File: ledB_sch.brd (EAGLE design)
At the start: 22.9 x 22.9 mm, 7 parts

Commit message: add image and fix schema
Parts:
- removed JP2: S+ S-, microbuilder:1X02_OVAL
- added U1: PIEZO, ledB_sch:1X02_PEIZO
- OPAMP: device linear:DIL08 -> ledB_sch:DIL08
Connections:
- net GND: now also R1.1, U1.1; no longer JP2.2
- net SIG: now also U1.2; no longer JP2.1
- net VCC: no longer R1.1
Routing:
- net SIG: track 25.0 -> 15.1 mm
- net GND: track 29.8 -> 26.2 mm
- net VCC: track 25.4 -> 22.2 mm

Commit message: add image and fix schema 2
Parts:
- moved JP1 16.6 mm to (11.0, 19.7), turned to 0 degrees
- moved LED1 16.4 mm to (11.0, 3.24), turned to 180 degrees
- moved D1 16.1 mm to (17.4, 7.05), turned to 90 degrees
- moved R2 14.8 mm to (18.4, 14.9), turned to 115 degrees
- moved R1 13.1 mm to (4.28, 7.16), turned to 115 degrees
- moved U1 12.1 mm to (3.57, 15.5), turned to 78 degrees
- moved OPAMP 1.47 mm to (11.0, 12.1), turned to 270 degrees
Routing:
- net N$1: track 3.59 -> 26.7 mm
- net VCC: track 22.2 -> 14.9 mm
- net N$5: track 10.1 -> 5.59 mm
- net GND: track 26.2 -> 30.1 mm
- net N$2: track 9.97 -> 6.47 mm
- net SIG: track 15.1 -> 16.9 mm

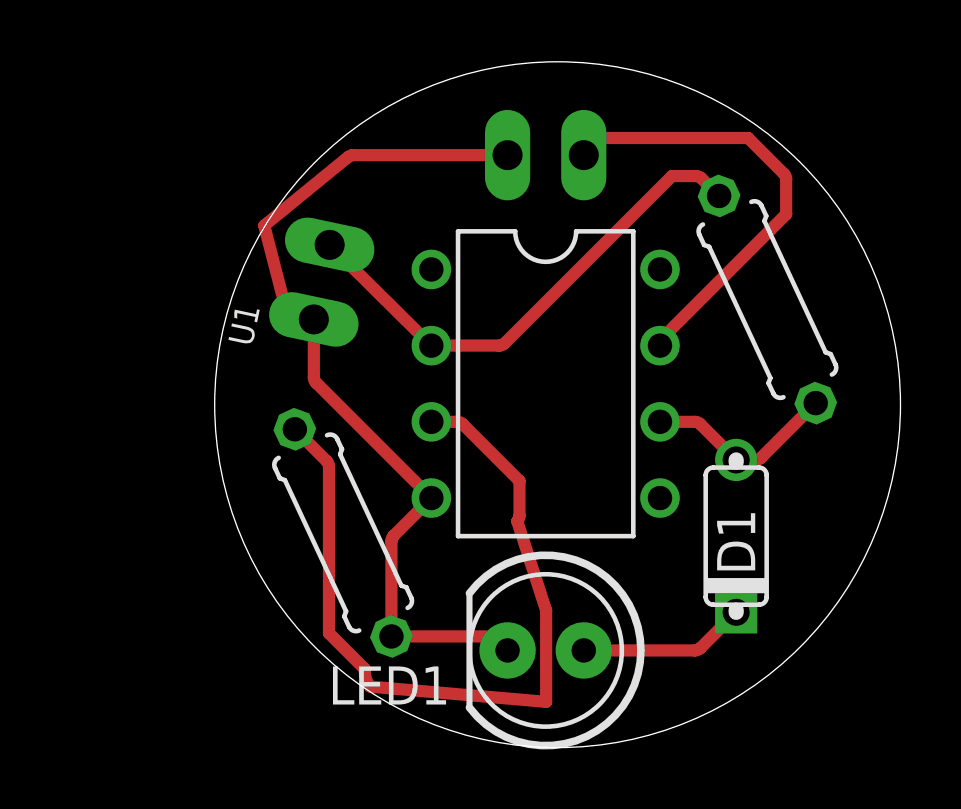
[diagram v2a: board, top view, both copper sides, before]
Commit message: added topoR assited routing
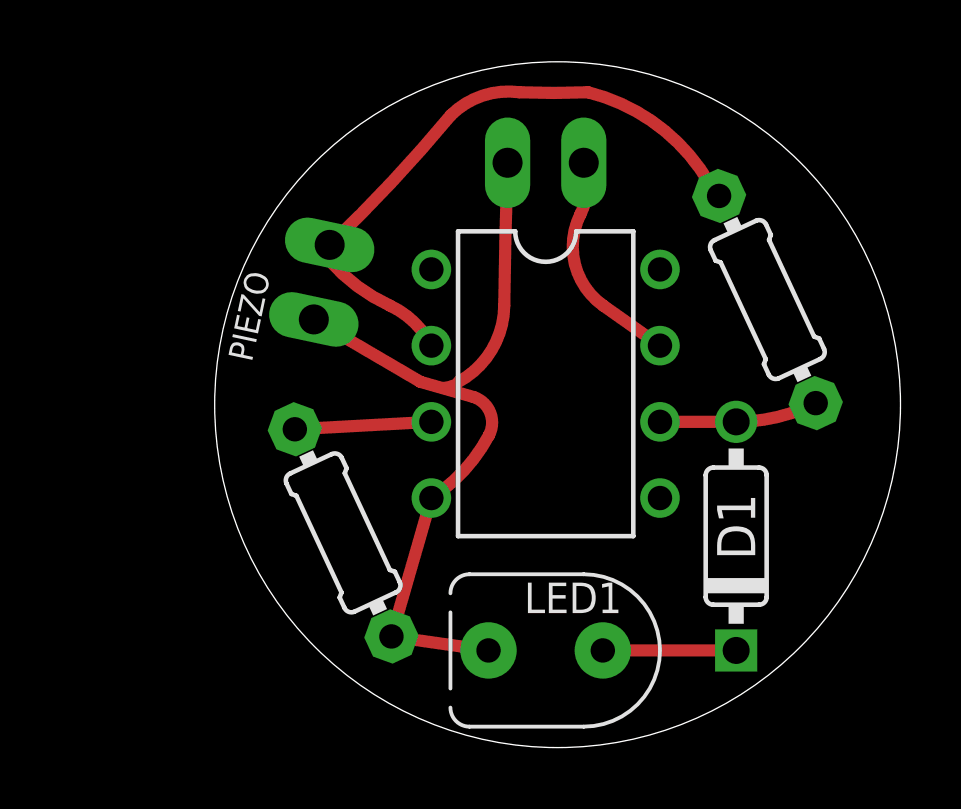
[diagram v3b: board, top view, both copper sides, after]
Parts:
- D1: value 1N4148-2 -> diode; device gm-diodes:DO35-2 -> ledB_sch:DO35-3
- JP1: value 6V+ GND -> 6V+; device microbuilder:1X02_OVAL -> ledB_sch:1X02_OVAL
- LED1: device SparkFun-LED:LED5MM -> ledB_sch:LED5MM
- R1, R2: device adafruit:0207/7 -> ledB_sch:0204/7
- moved JP1 0.25 mm to (11.0, 19.5)
- renumbered U1 to PIEZO
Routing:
- net N$1: track 26.7 -> 4.56 mm
- net VCC: track 14.9 -> 7.17 mm
- net SIG: track 16.9 -> 21.3 mm
- net GND: track 30.1 -> 27.2 mm
- net N$2: track 6.47 -> 5.26 mm
- net N$5: track 5.59 -> 4.44 mm
